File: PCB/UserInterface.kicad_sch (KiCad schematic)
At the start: 8 parts, among them J10 B2B-PH-K-S, J11 B2B-PH-K-S, J2 Conn_01x12, J3 Conn_01x16, J9 B3B-PH-K-S

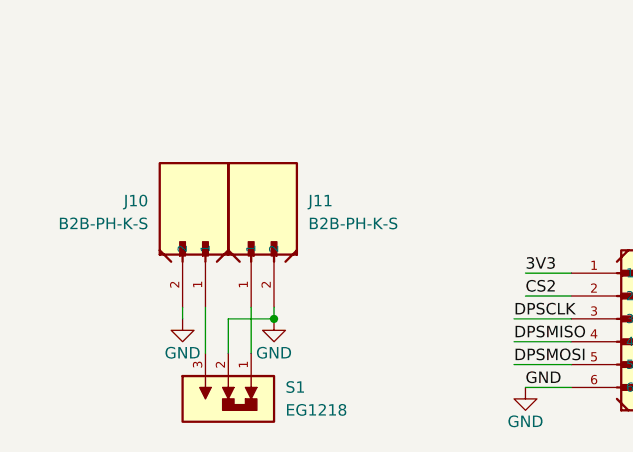
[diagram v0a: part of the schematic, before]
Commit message: Add files via upload
Updated Sizing on User Interface
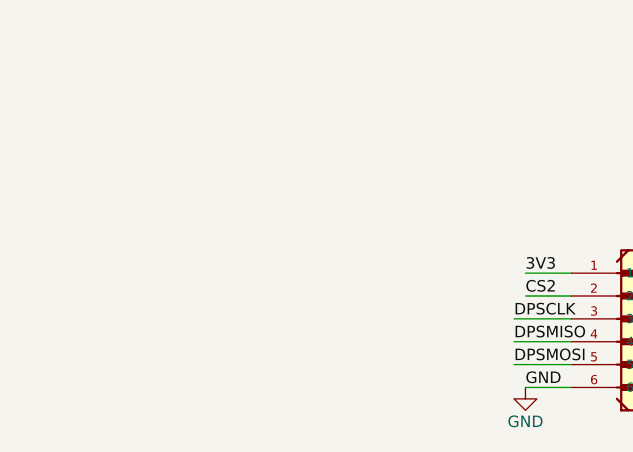
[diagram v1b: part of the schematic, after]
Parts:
- removed J10, J11: B2B-PH-K-S, B2B_PH_K_S:JST_B2B-PH-K-S, symbol B2B-PH-K-S:B2B-PH-K-S
- removed S1: EG1218, EG1218:SW_EG1218, symbol EG1218:EG1218
